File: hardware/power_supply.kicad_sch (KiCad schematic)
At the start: 27 parts, among them U2 BD50FC0FP, U3 BD50FC0FP, U4 LM62440-Q1, U5 TLV743P

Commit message: Add the Cube project
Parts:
- removed L?: 6u8, Inductor_SMD:L_Vishay_IHLP-1616, symbol Traction_Control_System-rescue:L_Core_Ferrite-Device
- added L2: 6u8, symbol Device:L_Ferrite
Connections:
- net +3.3VA: now also L2.2
- net +3V3 renamed +3.3V
- net +3.3V: now also L2.1
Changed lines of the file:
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@@
   (paper "A4")
   (title_block
-    (date "2023-06-06")
+    (date "2023-07-01")
     (rev "${REVISION}")
     (company "Author: I. Kajdan")
@@
     (stroke (width 0) (type default))
   )
-  (wire (pts (xy 186.69 116.84) (xy 185.42 116.84))
-    (stroke (width 0) (type default))
-  )
   (wire (pts (xy 184.15 66.04) (xy 184.15 64.77))
     (stroke (width 0) (type default))
@@
     (stroke (width 0) (type default))
   )
-  (wire (pts (xy 137.16 158.75) (xy 137.16 161.29))
-    (stroke (width 0) (type default))
-  )
   (wire (pts (xy 86.36 53.34) (xy 86.36 54.61))
     (stroke (width 0) (type default))
@@
   )
   (wire (pts (xy 160.02 118.11) (xy 160.02 116.84))
+    (stroke (width 0) (type default))
+  )
+  (wire (pts (xy 137.16 161.29) (xy 139.7 161.29))
     (stroke (width 0) (type default))
   )
@@
     (effects (font (size 1.27 1.27)) (justify left bottom))
   )
-  (global_label "5V_AUX" (shape output) (at 137.16 158.75 90) (fields_autoplaced)
+  (global_label "5V_AUX" (shape output) (at 139.7 161.29 0) (fields_autoplaced)
     (effects (font (size 1.27 1.27)) (justify left))
-    (property "Intersheetrefs" "${INTERSHEET_REFS}" (at 137.16 148.9499 90)
+    (property "Intersheetrefs" "${INTERSHEET_REFS}" (at 149.5001 161.29 0)
       (effects (font (size 1.27 1.27)) (justify left) hide)
     )
@@
     )
   )
-  (symbol (lib_id "power:+7V") (at 184.15 64.77 0) (unit 1)
-    (in_bom yes) (on_board yes) (dnp no) (fields_autoplaced)
-    (property "Reference" "#PWR041" (at 184.15 68.58 0)
+  (symbol (lib_id "POWER_7V:+7V") (at 184.15 64.77 0) (unit 1)
+    (in_bom yes) (on_board yes) (dnp no) (fields_autoplaced)
+    (property "Reference" "#PWR0212" (at 184.15 68.58 0)
       (effects (font (size 1.27 1.27)) hide)
     )
@@
       (project "rearbox"
         (path "/b652b05a-4e3d-4ad1-b032-18886abe7d45/7045152e-d7a2-42d7-9b15-138e7f2928ca"
-          (reference "#PWR041") (unit 1)
+          (reference "#PWR0212") (unit 1)
         )
       )
@@
     )
   )
-  (symbol (lib_id "power:+3V3") (at 185.42 115.57 0) (unit 1)
+  (symbol (lib_id "power:+3.3V") (at 185.42 115.57 0) (unit 1)
     (in_bom yes) (on_board yes) (dnp no) (fields_autoplaced)
     (property "Reference" "#PWR010" (at 185.42 119.38 0)
       (effects (font (size 1.27 1.27)) hide)
     )
-    (property "Value" "+3V3" (at 185.42 111.76 0)
+    (property "Value" "+3.3V" (at 185.42 112.014 0)
       (effects (font (size 1.27 1.27)))
     )
@@
     )
   )
-  (symbol (lib_id "power:+3V3") (at 210.82 115.57 0) (unit 1)
+  (symbol (lib_id "power:+3.3V") (at 210.82 115.57 0) (unit 1)
     (in_bom yes) (on_board yes) (dnp no) (fields_autoplaced)
     (property "Reference" "#PWR010" (at 210.82 119.38 0)
       (effects (font (size 1.27 1.27)) hide)
     )
-    (property "Value" "+3V3" (at 210.82 111.76 0)
+    (property "Value" "+3.3V" (at 210.82 112.014 0)
       (effects (font (size 1.27 1.27)))
     )
@@
     )
   )
-  (symbol (lib_id "power:+7V") (at 83.82 115.57 0) (unit 1)
-    (in_bom yes) (on_board yes) (dnp no) (fields_autoplaced)
-    (property "Reference" "#PWR020" (at 83.82 119.38 0)
+  (symbol (lib_id "POWER_7V:+7V") (at 83.82 115.57 0) (unit 1)
+    (in_bom yes) (on_board yes) (dnp no) (fields_autoplaced)
+    (property "Reference" "#PWR0214" (at 83.82 119.38 0)
       (effects (font (size 1.27 1.27)) hide)
     )
@@
       (project "rearbox"
         (path "/b652b05a-4e3d-4ad1-b032-18886abe7d45/7045152e-d7a2-42d7-9b15-138e7f2928ca"
-          (reference "#PWR020") (unit 1)
+          (reference "#PWR0214") (unit 1)
         )
       )
@@
     )
   )
-  (symbol (lib_id "power:+7V") (at 83.82 160.02 0) (unit 1)
-    (in_bom yes) (on_board yes) (dnp no) (fields_autoplaced)
-    (property "Reference" "#PWR021" (at 83.82 163.83 0)
+  (symbol (lib_id "POWER_7V:+7V") (at 83.82 160.02 0) (unit 1)
+    (in_bom yes) (on_board yes) (dnp no) (fields_autoplaced)
+    (property "Reference" "#PWR0213" (at 83.82 163.83 0)
       (effects (font (size 1.27 1.27)) hide)
     )
@@
       (project "rearbox"
         (path "/b652b05a-4e3d-4ad1-b032-18886abe7d45/7045152e-d7a2-42d7-9b15-138e7f2928ca"
-          (reference "#PWR021") (unit 1)
+          (reference "#PWR0213") (unit 1)
         )
       )
@@
   (symbol (lib_id "power:PWR_FLAG") (at 185.42 90.17 270) (unit 1)
     (in_bom yes) (on_board yes) (dnp no) (fields_autoplaced)
-    (property "Reference" "#FLG08" (at 187.325 90.17 0)
+    (property "Reference" "#FLG06" (at 187.325 90.17 0)
       (effects (font (size 1.27 1.27)) hide)
     )
@@
       (project "rearbox"
         (path "/b652b05a-4e3d-4ad1-b032-18886abe7d45/7045152e-d7a2-42d7-9b15-138e7f2928ca"
-          (reference "#FLG08") (unit 1)
+          (reference "#FLG06") (unit 1)
         )
       )
@@
   (symbol (lib_id "power:PWR_FLAG") (at 224.79 116.84 270) (unit 1)
     (in_bom yes) (on_board yes) (dnp no)
-    (property "Reference" "#FLG06" (at 226.695 116.84 0)
+    (property "Reference" "#FLG07" (at 226.695 116.84 0)
       (effects (font (size 1.27 1.27)) hide)
     )
@@
       (project "rearbox"
         (path "/b652b05a-4e3d-4ad1-b032-18886abe7d45/7045152e-d7a2-42d7-9b15-138e7f2928ca"
-          (reference "#FLG06") (unit 1)
+          (reference "#FLG07") (unit 1)
         )
         (path "/b652b05a-4e3d-4ad1-b032-18886abe7d45"
@@
     )
   )
+  (symbol (lib_id "Device:L_Ferrite") (at 217.17 116.84 90) (unit 1)
+    (in_bom yes) (on_board yes) (dnp no) (fields_autoplaced)
+    (property "Reference" "L2" (at 217.17 110.49 90)
+      (effects (font (size 1.27 1.27)))
+    )
+    (property "Value" "6u8" (at 217.17 113.03 90)
+      (effects (font (size 1.27 1.27)))
+    )
+    (property "Footprint" "" (at 217.17 116.84 0)
+      (effects (font (size 1.27 1.27)) hide)
+    )
+    (property "Datasheet" "~" (at 217.17 116.84 0)
+      (effects (font (size 1.27 1.27)) hide)
+    )
+    (pin "1")
+    (pin "2")
+    (instances
+      (project "rearbox"
+        (path "/b652b05a-4e3d-4ad1-b032-18886abe7d45/7045152e-d7a2-42d7-9b15-138e7f2928ca"
+          (reference "L2") (unit 1)
+        )
+      )
+    )
+  )
   (symbol (lib_id "Regulator_Linear:BD50FC0FP") (at 114.3 161.29 0) (unit 1)
     (in_bom yes) (on_board yes) (dnp no) (fields_autoplaced)
@@
         (path "/b652b05a-4e3d-4ad1-b032-18886abe7d45/7045152e-d7a2-42d7-9b15-138e7f2928ca"
           (reference "U3") (unit 1)
-        )
-      )
-    )
-  )
-  (symbol (lib_id "power:PWR_FLAG") (at 186.69 116.84 270) (unit 1)
-    (in_bom yes) (on_board yes) (dnp no)
-    (property "Reference" "#FLG07" (at 188.595 116.84 0)
-      (effects (font (size 1.27 1.27)) hide)
-    )
-    (property "Value" "PWR_FLAG" (at 190.5 116.84 90)
-      (effects (font (size 1.27 1.27)) (justify left))
-    )
-    (property "Footprint" "" (at 186.69 116.84 0)
-      (effects (font (size 1.27 1.27)) hide)
-    )
-    (property "Datasheet" "~" (at 186.69 116.84 0)
-      (effects (font (size 1.27 1.27)) hide)
-    )
-    (pin "1")
-    (instances
-      (project "rearbox"
-        (path "/b652b05a-4e3d-4ad1-b032-18886abe7d45/7045152e-d7a2-42d7-9b15-138e7f2928ca"
-          (reference "#FLG07") (unit 1)
-        )
-        (path "/b652b05a-4e3d-4ad1-b032-18886abe7d45"
-          (reference "#FLG?") (unit 1)
         )
       )
@@
         )
       )
-    )
-  )
-  (symbol (lib_id "Traction_Control_System-rescue:L_Core_Ferrite-Device") (at 217.17 116.84 90) (unit 1)
-    (in_bom yes) (on_board yes) (dnp no)
-    (property "Reference" "L?" (at 218.44 113.03 90)
-      (effects (font (size 1.27 1.27)) (justify left))
-    )
-    (property "Value" "6u8" (at 217.17 119.38 90)
-      (effects (font (size 1.27 1.27)))
-    )
-    (property "Footprint" "Inductor_SMD:L_Vishay_IHLP-1616" (at 217.17 116.84 0)
-      (effects (font (size 1.27 1.27)) hide)
-    )
-    (property "Datasheet" "~" (at 217.17 116.84 0)
-      (effects (font (size 1.27 1.27)) hide)
-    )
-    (pin "1")
-    (pin "2")
-    (instances
-      (project "rearbox"
-        (path "/b652b05a-4e3d-4ad1-b032-18886abe7d45"
-          (reference "L?") (unit 1)
-        )
-        (path "/b652b05a-4e3d-4ad1-b032-18886abe7d45/7045152e-d7a2-42d7-9b15-138e7f2928ca"
-          (reference "L2") (unit 1)
-        )
-      )
-      (project "Traction_Control_System"
-        (path "/f20670e0-69c0-4042-a790-cde4391abff4/00000000-0000-0000-0000-0000621459db"
-          (reference "L?") (unit 1)
-        )
-      )

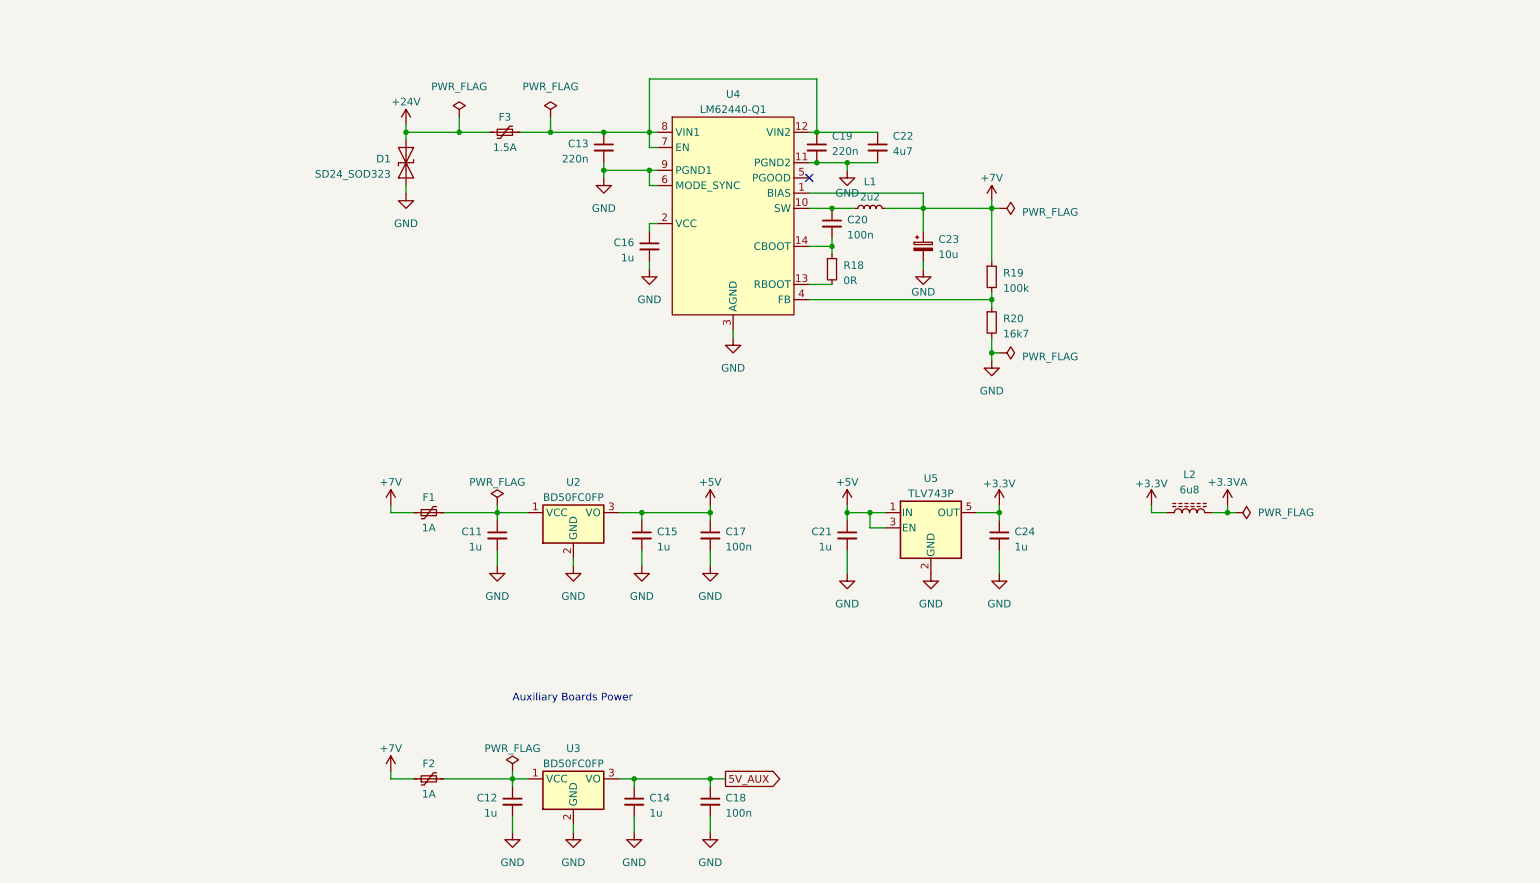
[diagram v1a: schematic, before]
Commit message: Improve the schematic
- add anti-aliasing filters
- rearrange the main connector signals
- improve the power filtering
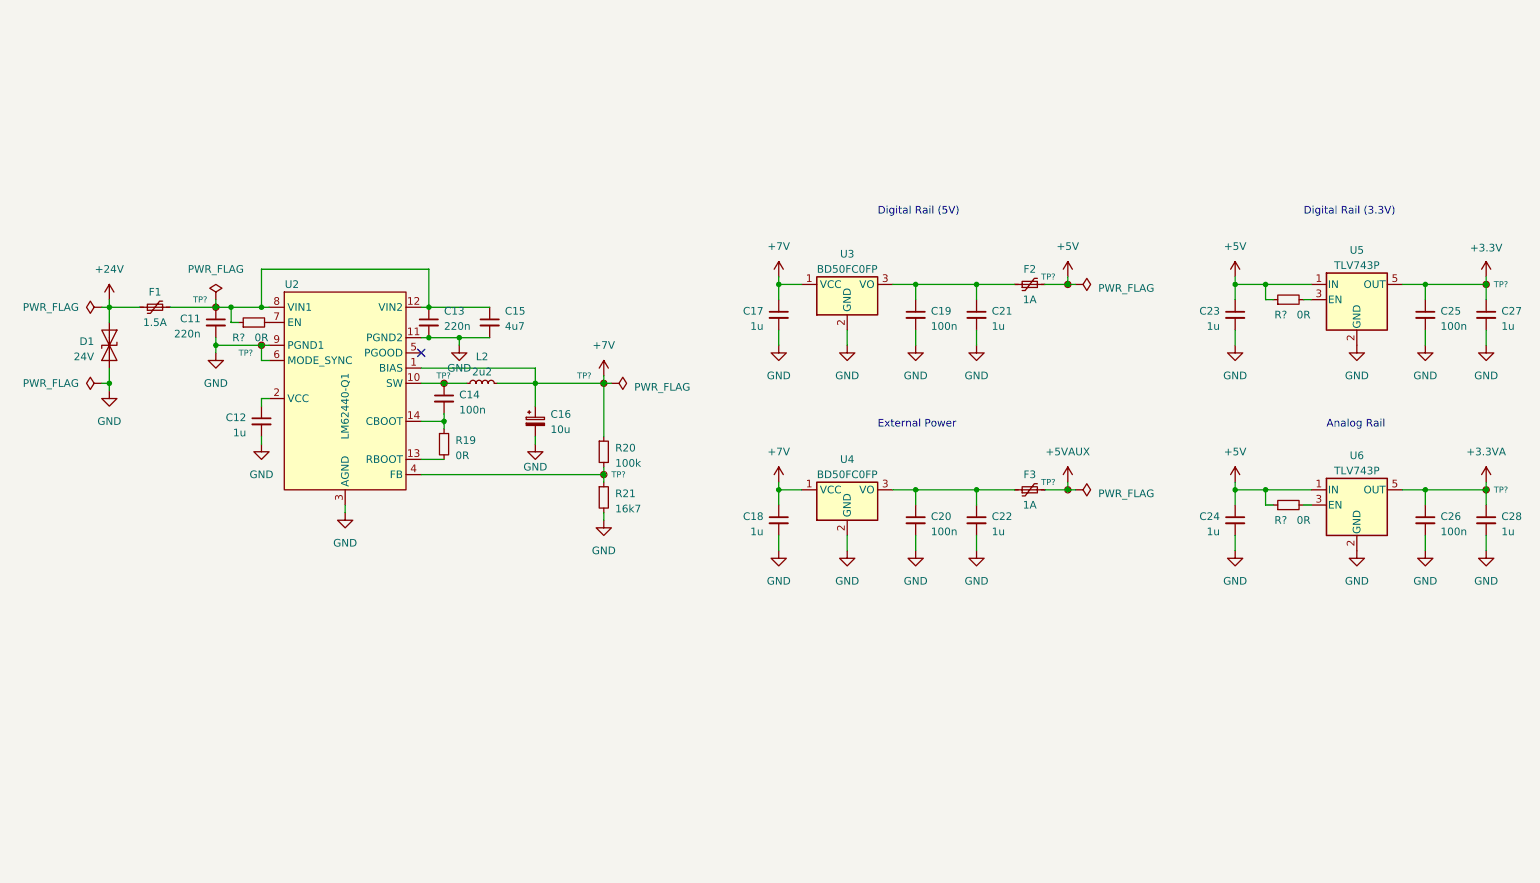
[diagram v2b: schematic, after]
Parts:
- removed C12, C14: 1u, Capacitor_SMD:C_0402_1005Metric_Pad0.74x0.62mm_HandSolder, symbol Device:C_Small
- removed F1: 1A, Fuse:Fuse_1812_4532Metric_Pad1.30x3.40mm_HandSolder, symbol Device:Polyfuse_Small
- removed L2: 6u8, symbol Device:L_Ferrite
- removed U3: BD50FC0FP, Package_TO_SOT_SMD:TO-252-2, symbol Regulator_Linear:BD50FC0FP
- added C20, C25, C26: 100n, Capacitor_SMD:C_0603_1608Metric, symbol Device:C_Small
- added C22, C24, C28: 1u, Capacitor_SMD:C_0603_1608Metric, symbol Device:C_Small
- added F2: 1A, Fuse:Fuse_0603_1608Metric, symbol Device:Polyfuse_Small
- added R? (x3): 0R, Resistor_SMD:R_0603_1608Metric, symbol Device:R_Small
- added TP? (x9): TestPoint_Small, TestPoint:TestPoint_Pad_D1.0mm, symbol Connector:TestPoint_Small
- added U4: BD50FC0FP, Package_TO_SOT_SMD:TO-252-2, symbol Regulator_Linear:BD50FC0FP
- added U6: TLV743P, Package_TO_SOT_SMD:SOT-23-5, symbol Regulator_Linear:TLV73330PDBV
- C11: renamed from C13; footprint Capacitor_SMD:C_0402_1005Metric_Pad0.74x0.62mm_HandSolder -> Capacitor_SMD:C_0603_1608Metric
- C12: renamed from C16; footprint Capacitor_SMD:C_0402_1005Metric_Pad0.74x0.62mm_HandSolder -> Capacitor_SMD:C_0603_1608Metric
- C13: renamed from C19; footprint Capacitor_SMD:C_0402_1005Metric_Pad0.74x0.62mm_HandSolder -> Capacitor_SMD:C_0603_1608Metric
- C14: renamed from C20; footprint Capacitor_SMD:C_0402_1005Metric_Pad0.74x0.62mm_HandSolder -> Capacitor_SMD:C_0603_1608Metric
- C17: renamed from C11; footprint Capacitor_SMD:C_0402_1005Metric_Pad0.74x0.62mm_HandSolder -> Capacitor_SMD:C_0603_1608Metric
- C18: value 100n -> 1u; footprint Capacitor_SMD:C_0402_1005Metric_Pad0.74x0.62mm_HandSolder -> Capacitor_SMD:C_0603_1608Metric
- C19: renamed from C17; footprint Capacitor_SMD:C_0402_1005Metric_Pad0.74x0.62mm_HandSolder -> Capacitor_SMD:C_0603_1608Metric
- C21: renamed from C15; footprint Capacitor_SMD:C_0402_1005Metric_Pad0.74x0.62mm_HandSolder -> Capacitor_SMD:C_0603_1608Metric
- C23: renamed from C21; footprint Capacitor_SMD:C_0402_1005Metric_Pad0.74x0.62mm_HandSolder -> Capacitor_SMD:C_0603_1608Metric
- C27: renamed from C24; footprint Capacitor_SMD:C_0402_1005Metric_Pad0.74x0.62mm_HandSolder -> Capacitor_SMD:C_0603_1608Metric
- D1: value SD24_SOD323 -> 24V; footprint Diode_SMD:D_SOD-323_HandSoldering -> (none)
- F1: renamed from F3; footprint Fuse:Fuse_0805_2012Metric -> Fuse:Fuse_0603_1608Metric
- F3: renamed from F2; footprint Fuse:Fuse_1812_4532Metric_Pad1.30x3.40mm_HandSolder -> Fuse:Fuse_0603_1608Metric
- R19: renamed from R18; footprint Resistor_SMD:R_0402_1005Metric -> Resistor_SMD:R_0603_1608Metric
- R20: renamed from R19; footprint Resistor_SMD:R_0402_1005Metric -> Resistor_SMD:R_0603_1608Metric
- R21: renamed from R20; footprint Resistor_SMD:R_0402_1005Metric -> Resistor_SMD:R_0603_1608Metric
- U2: renamed from U4; footprint Frontbox:IC_LM61460AANRJRR -> Local_Library:IC_LM61460AANRJRR; symbol LMR51420:LM62440 -> LM62440:LM62440
- U5: footprint Package_TO_SOT_SMD:SOT-23-5_HandSoldering -> Package_TO_SOT_SMD:SOT-23-5
- renumbered C22 to C15, C23 to C16, L1 to L2, U2 to U3
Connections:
- net 5V_AUX is gone; now on net +7V: C18.1
- net +3.3V: now also C25.1, TP?.1
- net +3.3VA: now also C26.1, C28.1, TP?.1, U6.5 (OUT)
- net +5V: now also C24.1, F2.2, R?.1, R?.1, TP?.1, U6.1 (IN); no longer C19.1, C21.1, U3.3 (VO), U5.3 (EN)
- net GND: now also C20.2, C22.2, C24.2, C25.2, C26.2, C28.2, TP?.1, U4.2 (GND), U6.2 (GND)
- net +7V: now reaches C17.1, U3.1 (VCC)
- net +7V: now also C16.1, L2.2, R20.1, U2.1 (BIAS), TP?.1, U4.1 (VCC)
- net at C14.1, L2.1, U2.10 (SW): now also TP?.1
- net at C11.1, C13.1, C15.1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: now also R?.1, TP?.1; no longer U2.7 (EN)
- net at R20.2, R21.1, U2.4 (FB): now also TP?.1
- net +5VAUX: now reaches F3.2
- net +5VAUX: now also TP?.1
- removed net +7.5V: C16.1, F3.1, L2.2, R20.1, U2.1 (BIAS)
- new net: C19.1, C21.1, F2.1, U3.3 (VO)
- new net: R?.2, U6.3 (EN)
- new net: R?.2, U2.7 (EN)
- new net: C20.1, C22.1, F3.1, U4.3 (VO)
- new net: R?.2, U5.3 (EN)
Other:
- note added: "Analog Rail"
- note added: "Digital Rail (3.3V)"
- note added: "Digital Rail (5V)"
- note added: "External Power"
- note removed: "Auxiliary Boards Power"
- moved on the sheet: C11, C12, C13, C14, C15, C16, C17, C19, C21, C23, C27, D1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

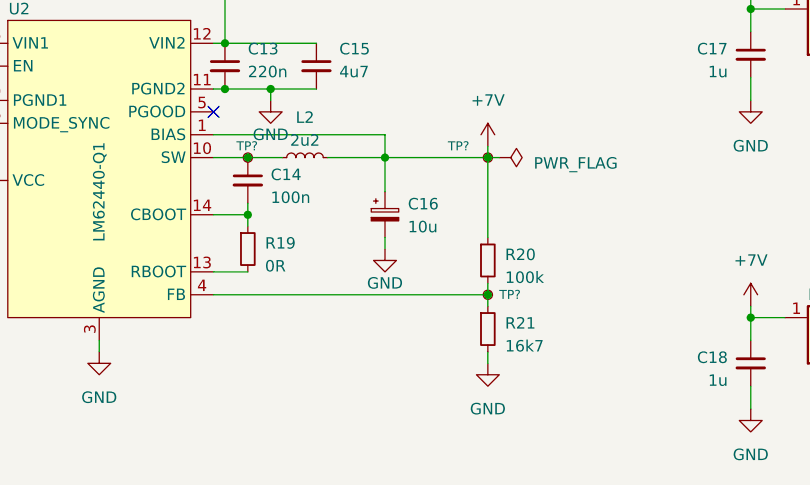
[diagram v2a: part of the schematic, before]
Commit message: Set component values
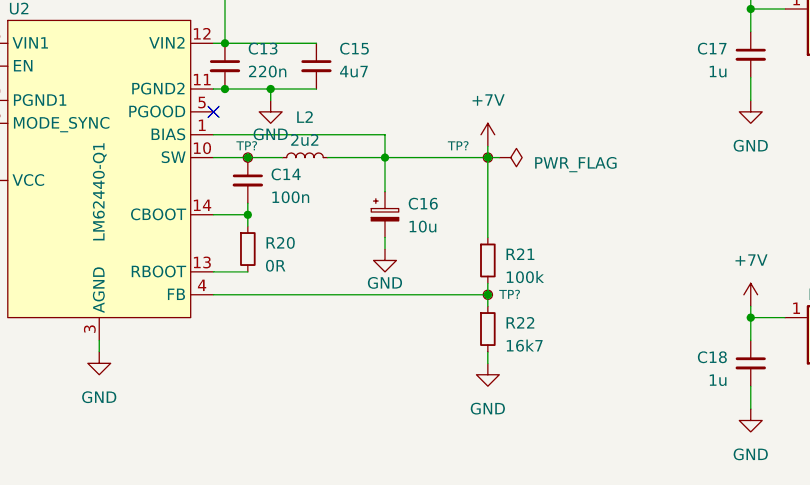
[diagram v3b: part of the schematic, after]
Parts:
- renumbered R19 to R20, R20 to R21, R21 to R22
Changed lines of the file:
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@@
         )
         (path "/b652b05a-4e3d-4ad1-b032-18886abe7d45/7045152e-d7a2-42d7-9b15-138e7f2928ca"
-          (reference "R23") (unit 1)
+          (reference "R24") (unit 1)
         )
       )
@@
   (symbol (lib_id "Device:R_Small") (at 92.71 105.41 0) (unit 1)
     (in_bom yes) (on_board yes) (dnp no) (fields_autoplaced)
-    (property "Reference" "R19" (at 94.615 104.775 0)
+    (property "Reference" "R20" (at 94.615 104.775 0)
       (effects (font (size 1.27 1.27)) (justify left))
     )
@@
       (project "rearbox"
         (path "/b652b05a-4e3d-4ad1-b032-18886abe7d45/7045152e-d7a2-42d7-9b15-138e7f2928ca"
-          (reference "R19") (unit 1)
+          (reference "R20") (unit 1)
         )
       )
@@
   (symbol (lib_id "Device:R_Small") (at 119.38 106.68 0) (unit 1)
     (in_bom yes) (on_board yes) (dnp no) (fields_autoplaced)
-    (property "Reference" "R20" (at 121.285 106.045 0)
+    (property "Reference" "R21" (at 121.285 106.045 0)
       (effects (font (size 1.27 1.27)) (justify left))
     )
@@
       (project "rearbox"
         (path "/b652b05a-4e3d-4ad1-b032-18886abe7d45/7045152e-d7a2-42d7-9b15-138e7f2928ca"
-          (reference "R20") (unit 1)
+          (reference "R21") (unit 1)
         )
       )
@@
         )
         (path "/b652b05a-4e3d-4ad1-b032-18886abe7d45/7045152e-d7a2-42d7-9b15-138e7f2928ca"
-          (reference "R18") (unit 1)
+          (reference "R19") (unit 1)
         )
       )
@@
         )
         (path "/b652b05a-4e3d-4ad1-b032-18886abe7d45/7045152e-d7a2-42d7-9b15-138e7f2928ca"
-          (reference "R22") (unit 1)
+          (reference "R23") (unit 1)
         )
       )
@@
   (symbol (lib_id "Device:R_Small") (at 119.38 114.3 0) (unit 1)
     (in_bom yes) (on_board yes) (dnp no) (fields_autoplaced)
-    (property "Reference" "R21" (at 121.285 113.665 0)
+    (property "Reference" "R22" (at 121.285 113.665 0)
       (effects (font (size 1.27 1.27)) (justify left))
     )
@@
       (project "rearbox"
         (path "/b652b05a-4e3d-4ad1-b032-18886abe7d45/7045152e-d7a2-42d7-9b15-138e7f2928ca"
-          (reference "R21") (unit 1)
-        )
-      )
+          (reference "R22") (unit 1)
+        )
+      )
